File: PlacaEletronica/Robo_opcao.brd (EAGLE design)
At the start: 139.7 x 153.7 mm, 102 parts, among them IC1 7805DT, IC2 7805DT, J2 S2B-PH-K-S(LF)(SN), J3 ZX62-B-5PA, J4 F-1X06-SIP-100-40, Q1 SMD-TRANSISTORS-NPN-25V-500MW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, Q2 SMD-TRANSISTORS-NPN-25V-500MW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, Q4 SFH_3716, Q5 TSOP4838, U1 ESP32-WROOM-32D, U2 AMS1117-3.3, U3 INTERFACE-CP2102-GMR(QFN28)QF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

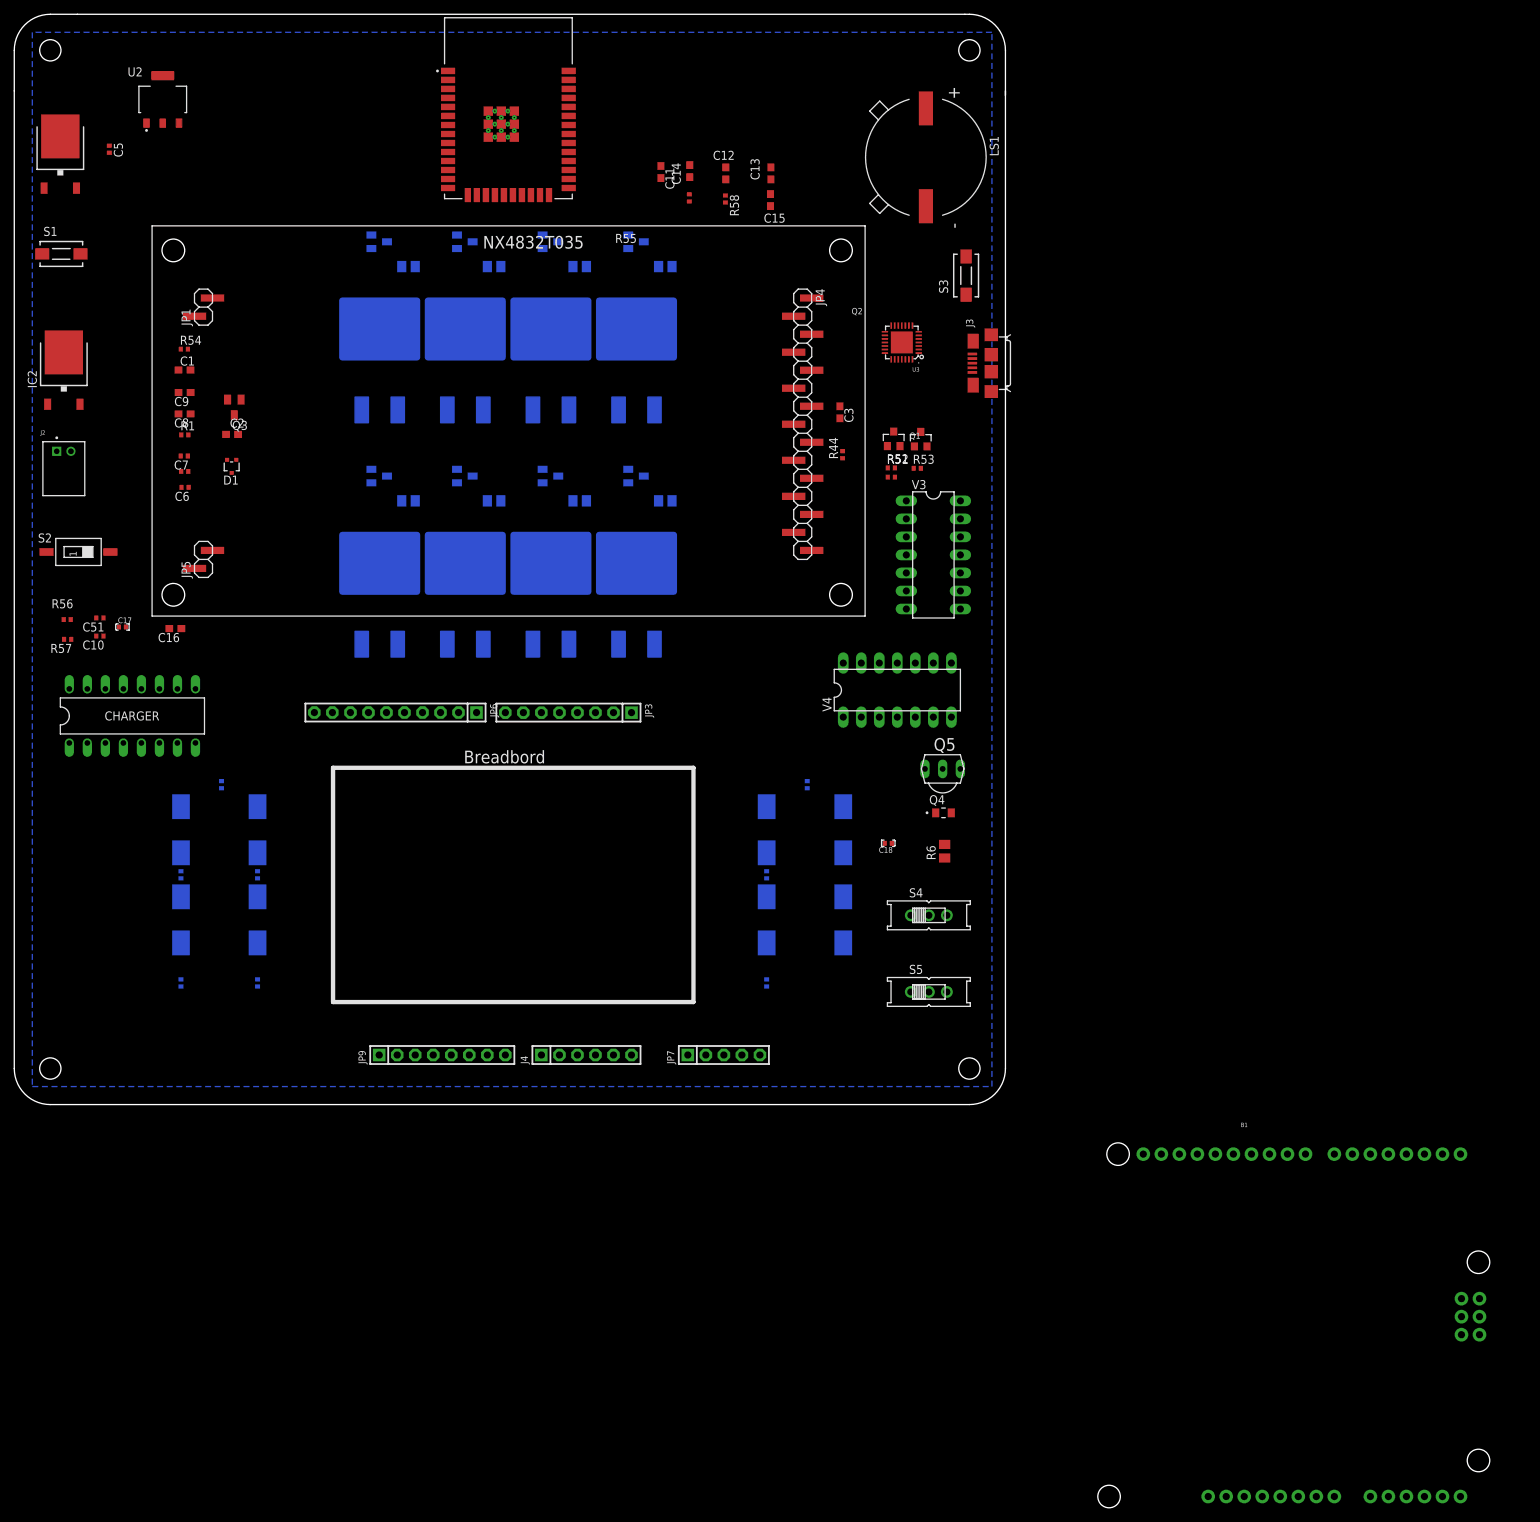
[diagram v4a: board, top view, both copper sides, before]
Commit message: [Modified] Placa principal - Buzzer e conector alimentacao
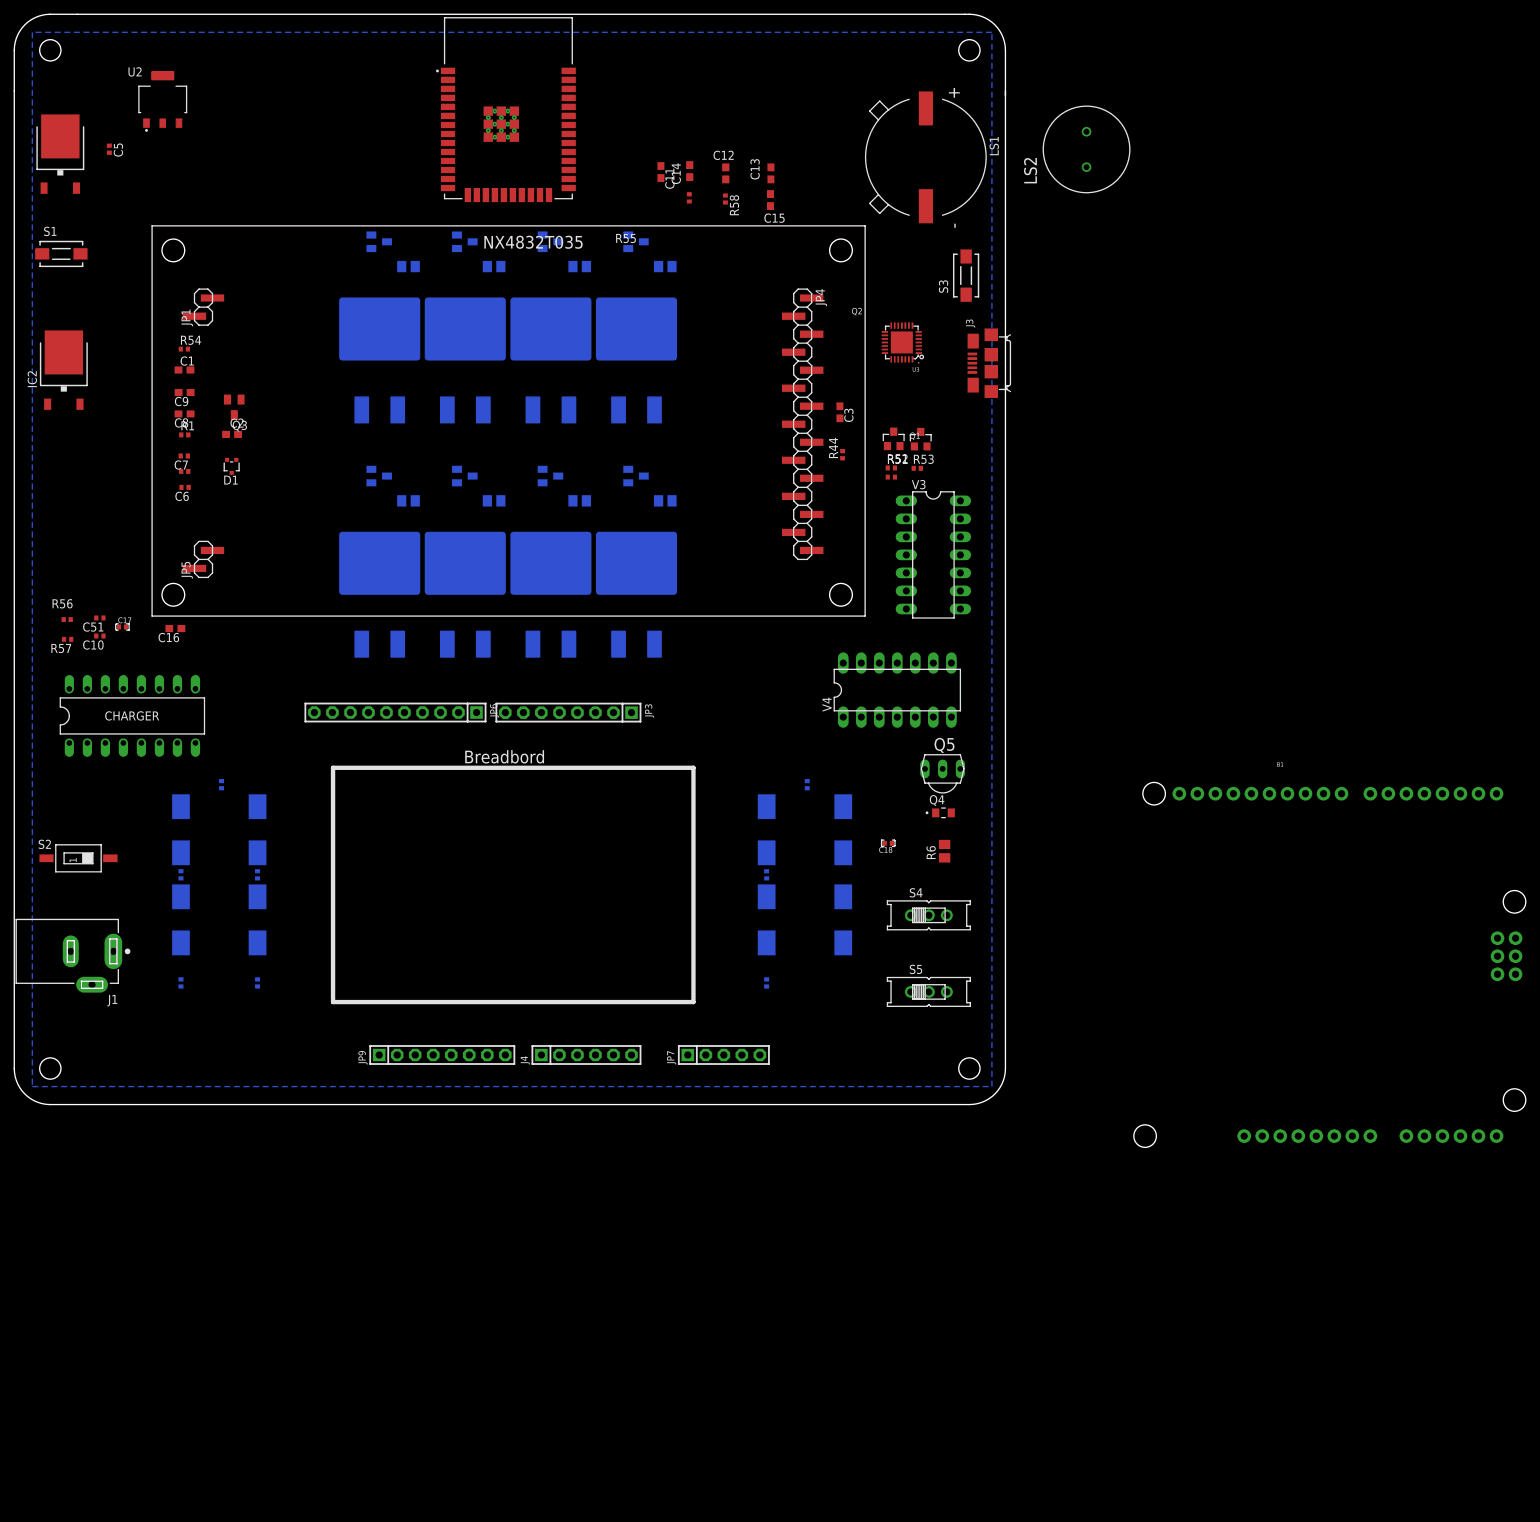
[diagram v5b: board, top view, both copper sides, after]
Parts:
- removed J2: S2B-PH-K-S(LF)(SN), S2B-PH-K-S_LF__SN_:JST_S2B-PH-K-S(LF)(SN)
- added J1: PJ-002A, PJ-002A:CUI_PJ-002A
- added LS2: PS1240P02BT, PS1240P02BT:XDCR_PS1240P02BT
- moved B1 51.1 mm to (178.4, 19.7)
- moved S2 43.2 mm to (9.05, 34.7)
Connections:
- removed net 5V: JP4.4
- removed net 5V(ATENçãO)-NãOESTACONECTADOEMNDA: JP9.5
- removed net 5V(NAOTACONECTADOEMNDA): JP9.2
- removed net GND_PWM~5V: C34.2, C35.+, C36.2, C37.+, C38.2, C39.+, C40.2, C41.+, C5.2, C6.1, D10.3, D11.3, D12.3, D13.3, IC1.2, U2.3, V3.14, V4.14
- new net GND_MOSFET: C34.2, C35.+, C36.2, C37.+, C38.2, C39.+, C40.2, C41.+, C5.2, C6.1, D10.3, D11.3, D12.3, D13.3, IC1.2, JP4.4, JP9.2, JP9.5, U2.3, V3.14, V4.14
- net B+: now also J1.1; no longer J2.2
- net BUZZER: now also LS2.2
- net GND: now also J1.3, LS2.1; no longer J2.1
